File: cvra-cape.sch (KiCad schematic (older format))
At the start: 27 parts, among them U3 BEAGLEBONE, U4 MCP251, U5 SN65HVD256, U6 SN65HVD256, X2 8Mhz

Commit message: Fix small details & replot pdf
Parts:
- removed unit 2 of U3
- removed unit 3 of U3
- removed unit 4 of U3
- removed unit 5 of U3
- added C6: 33n, symbol C_Small
- added R3: 0, symbol R_Small
- added unit 2 of U1
- added unit 3 of U1
- added unit 4 of U1
- added unit 5 of U1
- renumbered C6 to C1, C7 to C2, C8 to C3, C9 to C4, C10 to C5, CONN48 to CONN1, CONN49 to CONN2, CONN50 to CONN3, CONN51 to CONN4, CONN52 to CONN5, CONN53 to CONN6, D19 to D1, R52 to R1, R60 to R10, R53 to R2, R54 to R4, R55 to R5, R56 to R6, R57 to R7, R58 to R8, R59 to R9, U3 to U1, U4 to U2, U5 to U3, U6 to U4, X2 to X1
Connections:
- net labels added: D_IN_19, D_IN_20
- wire segments 106 -> 110
- no-connect marks 22 -> 44
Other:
- note added: "Maximum measurable \nvoltage is 19.8V on the bus\nResolution: 5mV\nTime-constant: 2.1ms"
- note removed: "Maximum measurable \nvoltage is 19.8V on the bus\nResolution: 5mV"
- moved on the sheet: CONN1, CONN2, R4, R5

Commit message: Update CAN power protection
Avoid dropout below 5V by using LTC4362 instead of custom protection with Shottky + Fuse
The chip provides overcurrent and overvoltage protection
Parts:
- removed D1: SBR130S3, symbol D_Schottky_Small
- removed F1: 0ZCH0075FF2G, symbol F_Small
- added C18: 10u, symbol C_Small
- added D1: CAN_PWR, symbol LED
- added R64: 1k, symbol R
- added U7: LTC4362, symbol LTC4362
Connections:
- wire segments 110 -> 138
- no-connect marks 44 -> 47
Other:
- moved on the sheet: C4, C6, CONN3, CONN4, R7, R8, R9, U3

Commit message: Add a recharge circuit for the RTC backup battery
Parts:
- C1, C18, C2, C3, C4, C5, C6: footprint (none) -> _std:_0603
- CONN1, CONN2, CONN3, CONN4, CONN5, CONN6: footprint MODULE -> _connectors:_Molex-PicoBlade-SMD-4
- U3, U4: footprint MODULE -> (none)

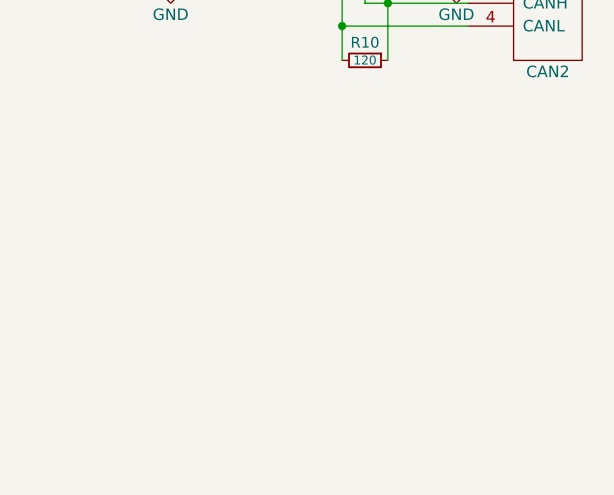
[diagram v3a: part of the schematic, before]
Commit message: Add CVRA logo to schematic
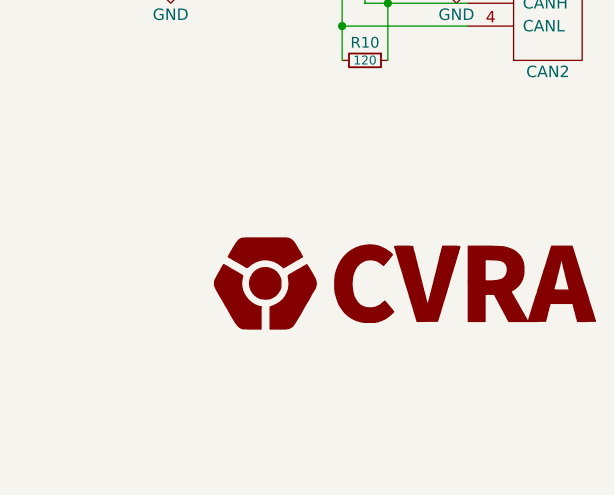
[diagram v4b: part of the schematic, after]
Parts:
- R1, R10, R2, R3, R4, R5, R6, R64, R7, R8, R9: footprint (none) -> _std:_0603
- U1: footprint (none) -> _beaglebone:BEAGLEBONE
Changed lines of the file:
@@
 EESchema Schematic File Version 2
+LIBS:cvra-cape-cache
 LIBS:power
 LIBS:device
@@
 LIBS:_transceiver
 LIBS:_wireless
-LIBS:cvra-cape-cache
 EELAYER 25 0
 EELAYER END
@@
 F 0 "U1" H 1025 1975 60  0000 C CNN
 F 1 "BEAGLEBONE" H 1425 1975 60  0000 C CNN
-F 2 "" H 975 2025 60  0001 C CNN
+F 2 "_beaglebone:BEAGLEBONE" H 975 2025 60  0001 C CNN
 F 3 "" H 975 2025 60  0000 C CNN
 	1    975  2025
@@
 F 0 "R9" V 10000 4025 47  0000 C BNN
 F 1 "120" V 10050 4025 39  0000 C CNN
-F 2 "" H 10050 4025 60  0001 C CNN
+F 2 "_std:_0603" H 10050 4025 60  0001 C CNN
 F 3 "" H 10050 4025 60  0000 C CNN
 	1    10050 4025
@@
 F 0 "R1" H 1430 3045 50  0000 L CNN
 F 1 "4.7k" H 1430 2985 50  0000 L CNN
-F 2 "" H 1400 3025 50  0001 C CNN
+F 2 "_std:_0603" H 1400 3025 50  0001 C CNN
 F 3 "" H 1400 3025 50  0000 C CNN
 	1    1400 3025
@@
 F 0 "R2" H 1680 3045 50  0000 L CNN
 F 1 "4.7k" H 1680 2985 50  0000 L CNN
-F 2 "" H 1650 3025 50  0001 C CNN
+F 2 "_std:_0603" H 1650 3025 50  0001 C CNN
 F 3 "" H 1650 3025 50  0000 C CNN
 	1    1650 3025
@@
 F 0 "R7" H 5184 6871 50  0000 L CNN
 F 1 "8.2k" H 5184 6779 50  0000 L CNN
-F 2 "" H 5125 6825 50  0001 C CNN
+F 2 "_std:_0603" H 5125 6825 50  0001 C CNN
 F 3 "" H 5125 6825 50  0000 C CNN
 	1    5125 6825
@@
 F 0 "R8" H 5184 7171 50  0000 L CNN
 F 1 "820" H 5184 7079 50  0000 L CNN
-F 2 "" H 5125 7125 50  0001 C CNN
+F 2 "_std:_0603" H 5125 7125 50  0001 C CNN
 F 3 "" H 5125 7125 50  0000 C CNN
 	1    5125 7125
@@
 F 0 "R10" V 10000 5850 47  0000 C BNN
 F 1 "120" V 10050 5850 39  0000 C CNN
-F 2 "" H 10050 5850 60  0001 C CNN
+F 2 "_std:_0603" H 10050 5850 60  0001 C CNN
 F 3 "" H 10050 5850 60  0000 C CNN
 	1    10050 5850
@@
 F 0 "R6" V 6350 4525 50  0000 C CNN
 F 1 "10k" V 6425 4525 50  0000 C CNN
-F 2 "" V 6355 4525 50  0001 C CNN
+F 2 "_std:_0603" V 6355 4525 50  0001 C CNN
 F 3 "" H 6425 4525 50  0000 C CNN
 	1    6425 4525
@@
 F 0 "R4" V 4125 5125 39  0000 C BNN
 F 1 "330" V 4175 5125 39  0000 C CNN
-F 2 "" H 4175 5125 50  0001 C CNN
+F 2 "_std:_0603" H 4175 5125 50  0001 C CNN
 F 3 "" H 4175 5125 50  0000 C CNN
 	1    4175 5125
@@
 F 0 "R5" V 4275 5225 39  0000 C BNN
 F 1 "330" V 4175 5225 39  0000 C CNN
-F 2 "" H 4175 5225 50  0001 C CNN
+F 2 "_std:_0603" H 4175 5225 50  0001 C CNN
 F 3 "" H 4175 5225 50  0000 C CNN
 	1    4175 5225
@@
 F 0 "R3" V 3950 5950 39  0000 C BNN
 F 1 "0" V 4000 5950 39  0000 C CNN
-F 2 "" H 4000 5950 50  0001 C CNN
+F 2 "_std:_0603" H 4000 5950 50  0001 C CNN
 F 3 "" H 4000 5950 50  0000 C CNN
 	1    4000 5950
@@
 F 0 "U1" H 2875 3400 60  0000 L CNN
 F 1 "BEAGLEBONE" H 3150 3400 60  0000 L CNN
-F 2 "" H 2925 3400 60  0001 C CNN
+F 2 "_beaglebone:BEAGLEBONE" H 2925 3400 60  0001 C CNN
 F 3 "" H 2925 3400 60  0000 C CNN
 	2    2925 3400
@@
 F 0 "U1" H 3875 3300 60  0000 L CNN
 F 1 "BEAGLEBONE" H 4125 3300 60  0000 L CNN
-F 2 "" H 3925 3350 60  0001 C CNN
+F 2 "_beaglebone:BEAGLEBONE" H 3925 3350 60  0001 C CNN
 F 3 "" H 3925 3350 60  0000 C CNN
 	3    3925 3350
@@
 F 0 "U1" H 5700 3300 60  0000 L CNN
 F 1 "BEAGLEBONE" H 6000 3300 60  0000 L CNN
-F 2 "" H 5750 3350 60  0001 C CNN
+F 2 "_beaglebone:BEAGLEBONE" H 5750 3350 60  0001 C CNN
 F 3 "" H 5750 3350 60  0000 C CNN
 	4    5750 3350
@@
 F 0 "U1" H 6750 3300 60  0000 L CNN
 F 1 "BEAGLEBONE" H 7025 3300 60  0000 L CNN
-F 2 "" H 6800 3350 60  0001 C CNN
+F 2 "_beaglebone:BEAGLEBONE" H 6800 3350 60  0001 C CNN
 F 3 "" H 6800 3350 60  0000 C CNN
 	5    6800 3350
@@
 F 0 "R64" H 10345 1871 50  0000 L CNN
 F 1 "1k" H 10345 1779 50  0000 L CNN
-F 2 "" V 10205 1825 50  0001 C CNN
+F 2 "_std:_0603" V 10205 1825 50  0001 C CNN
 F 3 "" H 10275 1825 50  0000 C CNN
 	1    10275 1825
@@
 NoConn ~ 8925 1550
 NoConn ~ 8925 1750
+$Comp
+L CVRA_logo #G?
+U 1 1 56D200EA
+P 10225 6825
+F 0 "#G?" H 10225 6657 60  0001 C CNN
+F 1 "CVRA_logo" H 10225 6993 60  0001 C CNN
+F 2 "" H 10225 6825 60  0000 C CNN
+F 3 "" H 10225 6825 60  0000 C CNN
+	1    10225 6825
+	1    0    0    -1
+$EndComp
 $EndSCHEMATC

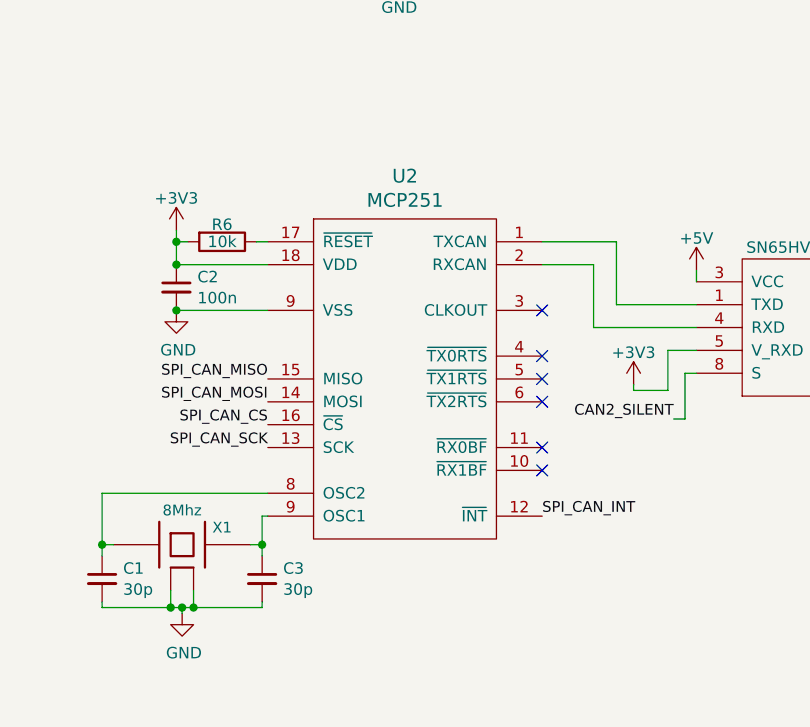
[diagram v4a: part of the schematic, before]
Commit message: Associate footprints
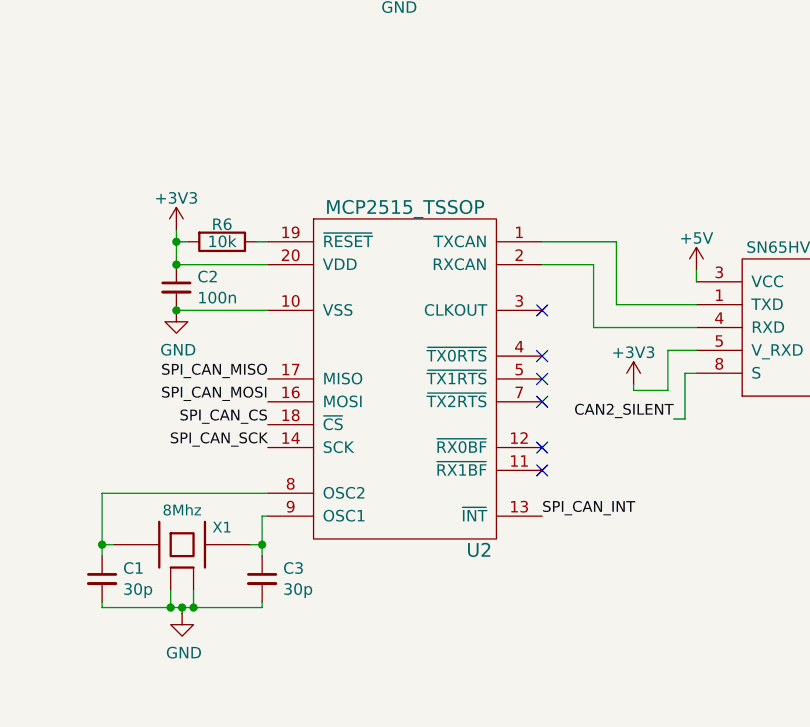
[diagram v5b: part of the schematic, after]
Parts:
- removed U2: MCP251, symbol MCP251
- added U2: MCP2515_TSSOP, Housings_SSOP:TSSOP-20_4.4x6.5mm_Pitch0.65mm, symbol MCP2515_TSSOP
- D1: footprint (none) -> _std:_0603
- U3, U4: footprint (none) -> _std:_SO-8
- U7: footprint (none) -> _dfn:DFN_8-Lead_2mmx3mm
- X1: footprint (none) -> _div:XTAL_ABMM2
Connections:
- net +3V3: now also U2.20 (VDD)
- net GND: now also U2.10 (VSS)
- net SPI_CAN_CS: now also U2.18 (~CS)
- net SPI_CAN_INT: now also U2.13 (~INT)
- net SPI_CAN_MISO: now also U2.17 (MISO)
- net SPI_CAN_MOSI: now also U2.16 (MOSI)
- net SPI_CAN_SCK: now also U2.14 (SCK)
- net at U4.1 (TXD): now also U2.1 (TXCAN)
- net at U4.4 (RXD): now also U2.2 (RXCAN)
- net at R6.1: now also U2.19 (~RESET)
- net at C1.1, X1.1: now also U2.8 (OSC2)
- net at C3.1, X1.3: now also U2.9 (OSC1)
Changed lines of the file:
@@
 F 0 "U3" H 9600 3425 50  0000 C CNN
 F 1 "SN65HVD256" H 8950 3425 50  0000 C CNN
-F 2 "" H 9200 3075 50  0001 C CNN
+F 2 "_std:_SO-8" H 9200 3075 50  0001 C CNN
 F 3 "CAN Transceiver" H 9200 3175 50  0001 C CNN
 	1    9200 3075
@@
 F 0 "U4" H 9600 5250 50  0000 C CNN
 F 1 "SN65HVD256" H 8950 5250 50  0000 C CNN
-F 2 "" H 9200 4900 50  0001 C CNN
+F 2 "_std:_SO-8" H 9200 4900 50  0001 C CNN
 F 3 "CAN Transceiver" H 9200 5000 50  0001 C CNN
 	1    9200 4900
@@
 CAN2_SILENT
 $Comp
-L MCP251 U2
-U 1 1 56AF9BEE
-P 7225 5075
-F 0 "U2" H 7225 5912 60  0000 C CNN
-F 1 "MCP251" H 7225 5806 60  0000 C CNN
-F 2 "" H 7375 5275 60  0001 C CNN
-F 3 "" H 7375 5275 60  0000 C CNN
-	1    7225 5075
-	1    0    0    -1
-$EndComp
-$Comp
 L XTAL-SMD-4-PADS X1
 U 1 1 56AF9E17
@@
 F 0 "X1" H 6425 5925 47  0000 C CNN
 F 1 "8Mhz" H 6250 6000 47  0000 C CNN
-F 2 "" H 6250 5850 60  0001 C CNN
+F 2 "_div:XTAL_ABMM2" H 6250 5850 60  0001 C CNN
 F 3 "" H 6250 5850 60  0000 C CNN
 	1    6250 5850
@@
 F 0 "U7" H 9675 750 60  0000 C CNN
 F 1 "LTC4362" H 9475 1850 60  0000 C CNN
-F 2 "" H 9475 1575 60  0001 C CNN
+F 2 "_dfn:DFN_8-Lead_2mmx3mm" H 9475 1575 60  0001 C CNN
 F 3 "" H 9475 1575 60  0000 C CNN
 	1    9475 1375
@@
 F 0 "D1" H 10025 1675 50  0000 C CNN
 F 1 "CAN_PWR" H 10025 1875 50  0000 C CNN
-F 2 "" H 10025 1775 50  0001 C CNN
+F 2 "_std:_0603" H 10025 1775 50  0001 C CNN
 F 3 "" H 10025 1775 50  0000 C CNN
 	1    10025 1775
@@
 NoConn ~ 8925 1750
 $Comp
-L CVRA_logo #G?
+L CVRA_logo #G1
 U 1 1 56D200EA
 P 10225 6825
-F 0 "#G?" H 10225 6657 60  0001 C CNN
+F 0 "#G1" H 10225 6657 60  0001 C CNN
 F 1 "CVRA_logo" H 10225 6993 60  0001 C CNN
 F 2 "" H 10225 6825 60  0000 C CNN
@@
 	1    0    0    -1
 $EndComp
+$Comp
+L MCP2515_TSSOP U2
+U 1 1 56D2E5AA
+P 7225 5075
+F 0 "U2" H 7550 4275 60  0000 C CNN
+F 1 "MCP2515_TSSOP" H 7225 5775 60  0000 C CNN
+F 2 "Housings_SSOP:TSSOP-20_4.4x6.5mm_Pitch0.65mm" H 7375 5275 60  0001 C CNN
+F 3 "" H 7375 5275 60  0000 C CNN
+	1    7225 5075
+	1    0    0    -1
+$EndComp

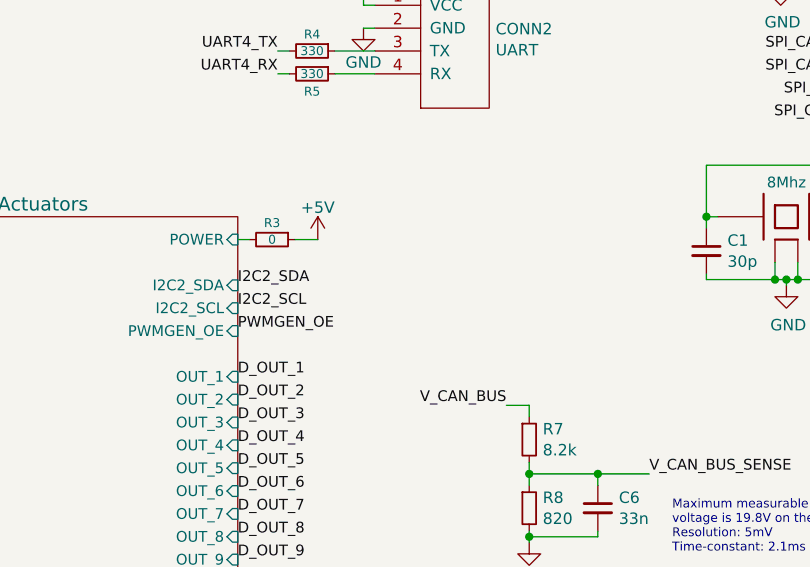
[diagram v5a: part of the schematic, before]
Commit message: Add Power connector for servos and silkscreen annotations
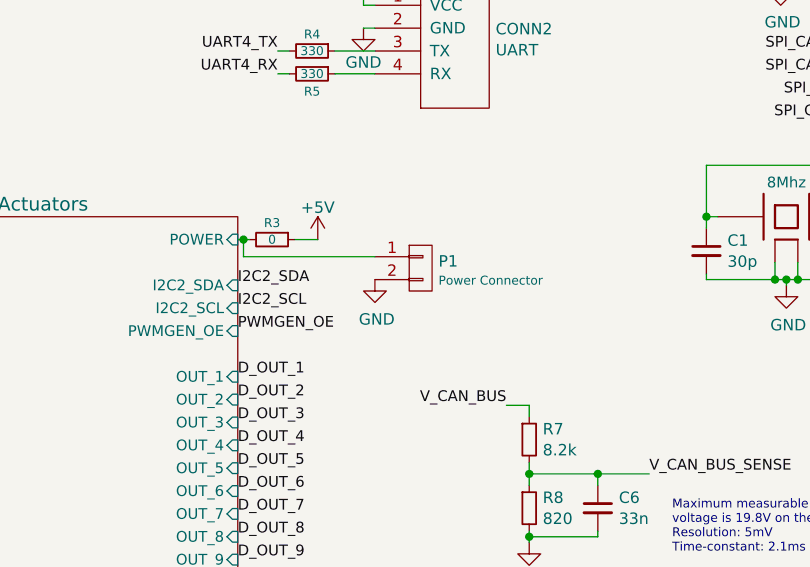
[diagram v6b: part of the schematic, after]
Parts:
- added P1: Power Connector, Pin_Headers:Pin_Header_Straight_1x02, symbol CONN_01X02
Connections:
- net Actuators/POWER: now also P1.1 (P1)
- net GND: now also P1.2 (P2)
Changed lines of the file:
@@
 Sheet 1 3
 Title "Goldorak cape"
-Date "2016-02-27"
+Date "2016-03-04"
 Rev "A"
 Comp "Club Vaudois de Robotique Autonome (CVRA)"
@@
 	4100 5950 4200 5950
 Wire Wire Line
-	3900 5950 3850 5950
+	3850 5950 3900 5950
 Connection ~ 5125 7250
 Wire Wire Line
@@
 	1    0    0    -1
 $EndComp
+$Comp
+L CONN_01X02 P1
+U 1 1 56D8CD8C
+P 4650 6075
+F 0 "P1" H 4728 6105 50  0000 L CNN
+F 1 "Power Connector" H 4728 6021 39  0000 L CNN
+F 2 "Pin_Headers:Pin_Header_Straight_1x02" H 4650 6075 50  0001 C CNN
+F 3 "" H 4650 6075 50  0000 C CNN
+	1    4650 6075
+	1    0    0    -1
+$EndComp
+Wire Wire Line
+	3875 5950 3875 6025
+Wire Wire Line
+	3875 6025 4450 6025
+Connection ~ 3875 5950
+$Comp
+L GND #PWR039
+U 1 1 56D8E9D7
+P 4450 6125
+F 0 "#PWR039" H 4450 5875 50  0001 C CNN
+F 1 "GND" H 4458 5951 50  0000 C CNN
+F 2 "" H 4450 6125 50  0000 C CNN
+F 3 "" H 4450 6125 50  0000 C CNN
+	1    4450 6125
+	1    0    0    -1
+$EndComp
